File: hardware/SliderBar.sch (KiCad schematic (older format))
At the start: 5 parts

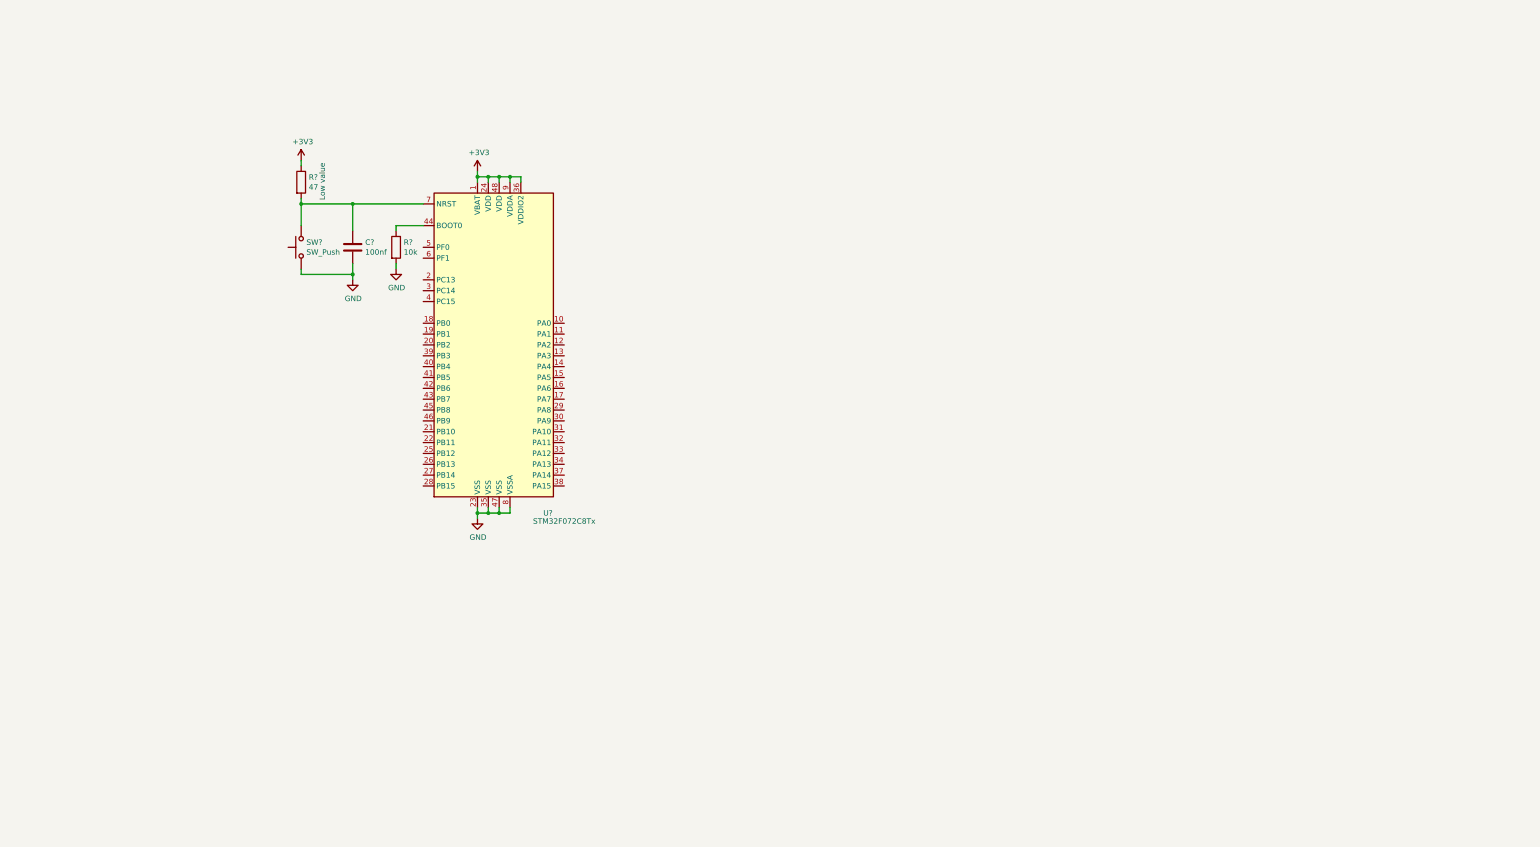
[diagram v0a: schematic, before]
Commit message: Add ULDO 3.3V regulator
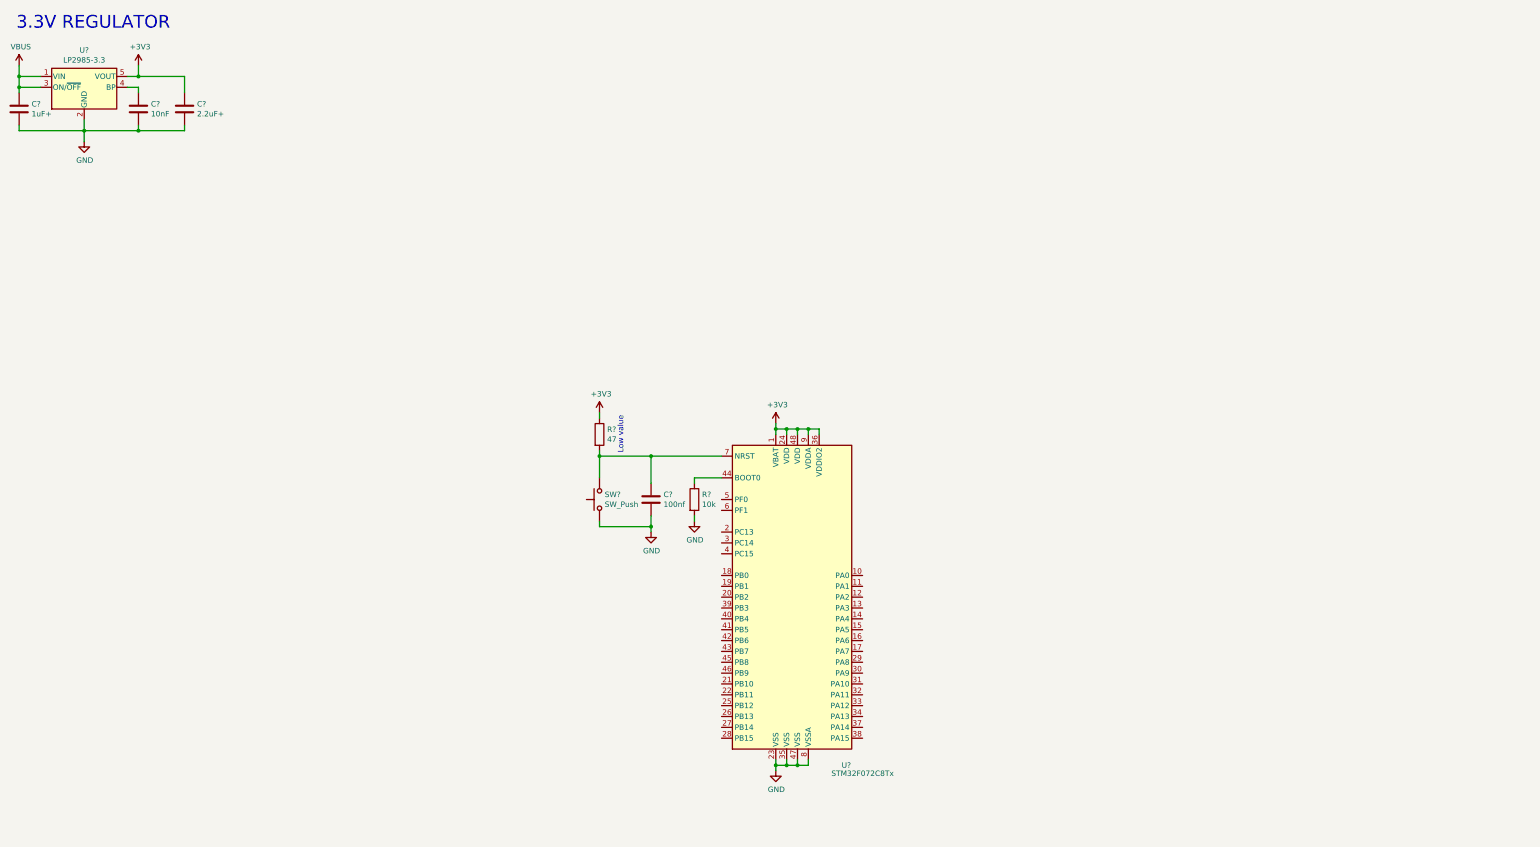
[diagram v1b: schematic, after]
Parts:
- added C?: 1uF+, symbol Device:C
- added C?: 10nF, symbol Device:C
- added C?: 2.2uF+, symbol Device:C
- added U?: LP2985-3.3, Package_TO_SOT_SMD:SOT-23-5, symbol Regulator_Linear:LP2985-3.3
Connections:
- net +3V3: now also C?.1, U?.5 (VOUT)
- net GND: now also C?.2, C?.2, C?.2, U?.2 (GND)
- new net: C?.1, U?.4 (BP)
- new net VBUS: C?.1, U?.1 (VIN), U?.3 (ON/~OFF~)
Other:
- note added: "3.3V REGULATOR"
- moved on the sheet: C?, R?, SW?, U?

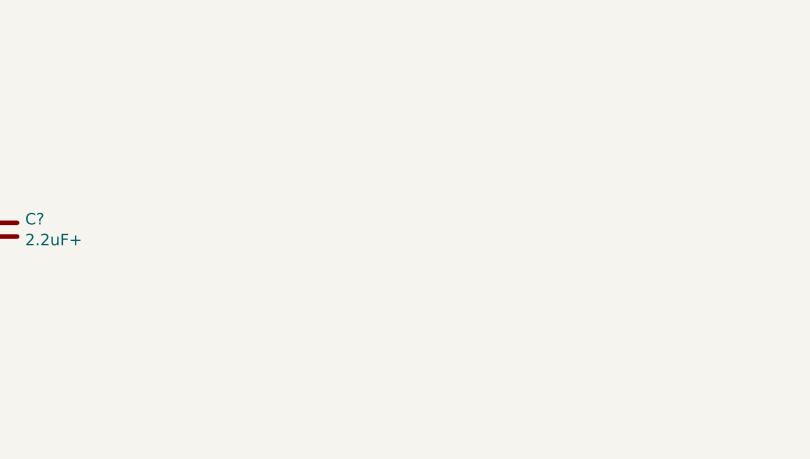
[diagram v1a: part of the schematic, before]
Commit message: Add power protection diodes
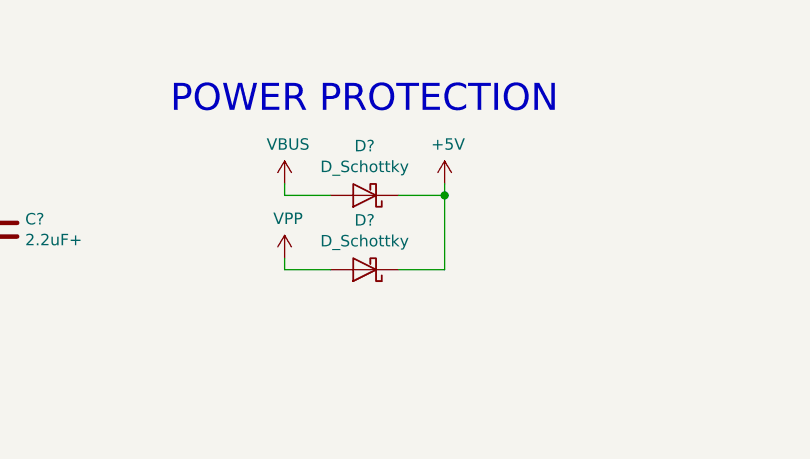
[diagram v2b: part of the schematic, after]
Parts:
- added D? (x2): D_Schottky, symbol Device:D_Schottky
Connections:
- net VBUS: now also D?.2 (A)
- new net +5V: D?.1 (K), D?.1 (K)
- new net VPP: D?.2 (A)
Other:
- note added: "POWER PROTECTION"
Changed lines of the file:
@@
 Text Notes 1300 950  0    118  ~ 0
 3.3V REGULATOR
+$Comp
+L power:VBUS #PWR?
+U 1 1 5D009DCE
+P 4100 1475
+F 0 "#PWR?" H 4100 1325 50  0001 C CNN
+F 1 "VBUS" H 4115 1648 50  0000 C CNN
+F 2 "" H 4100 1475 50  0001 C CNN
+F 3 "" H 4100 1475 50  0001 C CNN
+	1    4100 1475
+	1    0    0    -1
+$EndComp
+$Comp
+L power:VPP #PWR?
+U 1 1 5D00A59F
+P 4100 1800
+F 0 "#PWR?" H 4100 1650 50  0001 C CNN
+F 1 "VPP" H 4115 1973 50  0000 C CNN
+F 2 "" H 4100 1800 50  0001 C CNN
+F 3 "" H 4100 1800 50  0001 C CNN
+	1    4100 1800
+	1    0    0    -1
+$EndComp
+$Comp
+L Device:D_Schottky D?
+U 1 1 5D00B4CC
+P 4450 1525
+F 0 "D?" H 4450 1309 50  0000 C CNN
+F 1 "D_Schottky" H 4450 1400 50  0000 C CNN
+F 2 "" H 4450 1525 50  0001 C CNN
+F 3 "~" H 4450 1525 50  0001 C CNN
+	1    4450 1525
+	-1   0    0    1
+$EndComp
+$Comp
+L Device:D_Schottky D?
+U 1 1 5D00C48C
+P 4450 1850
+F 0 "D?" H 4450 1634 50  0000 C CNN
+F 1 "D_Schottky" H 4450 1725 50  0000 C CNN
+F 2 "" H 4450 1850 50  0001 C CNN
+F 3 "~" H 4450 1850 50  0001 C CNN
+	1    4450 1850
+	-1   0    0    1
+$EndComp
+Wire Wire Line
+	4100 1800 4100 1850
+Wire Wire Line
+	4100 1850 4300 1850
+Wire Wire Line
+	4100 1475 4100 1525
+Wire Wire Line
+	4100 1525 4300 1525
+$Comp
+L power:+5V #PWR?
+U 1 1 5D01175F
+P 4800 1475
+F 0 "#PWR?" H 4800 1325 50  0001 C CNN
+F 1 "+5V" H 4815 1648 50  0000 C CNN
+F 2 "" H 4800 1475 50  0001 C CNN
+F 3 "" H 4800 1475 50  0001 C CNN
+	1    4800 1475
+	1    0    0    -1
+$EndComp
+Wire Wire Line
+	4800 1475 4800 1525
+Wire Wire Line
+	4800 1525 4600 1525
+Wire Wire Line
+	4600 1850 4800 1850
+Wire Wire Line
+	4800 1850 4800 1525
+Connection ~ 4800 1525
+Text Notes 3600 1175 0    118  ~ 0
+POWER PROTECTION
 $EndSCHEMATC

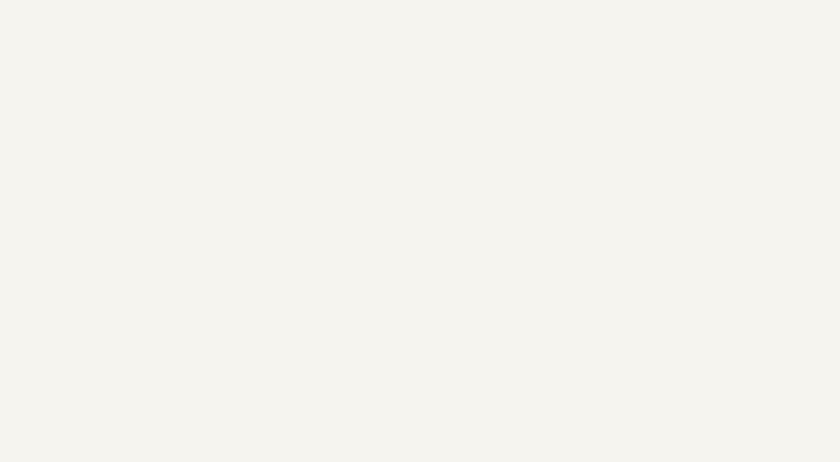
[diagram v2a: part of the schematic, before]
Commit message: Add decoupling caps
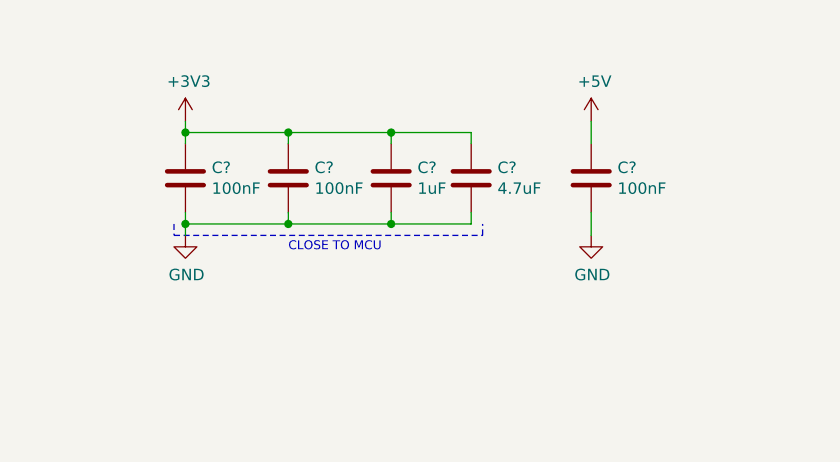
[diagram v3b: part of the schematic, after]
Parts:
- added C? (x3): 100nF, symbol Device:C
- added C?: 1uF, symbol Device:C
- added C?: 4.7uF, symbol Device:C
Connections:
- net +3V3: now also C?.1, C?.1, C?.1, C?.1
- net +5V: now also C?.1
- net GND: now also C?.2, C?.2, C?.2, C?.2, C?.2
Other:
- note added: "CLOSE TO MCU"
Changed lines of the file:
@@
 Text Notes 3600 1175 0    118  ~ 0
 POWER PROTECTION
+$Comp
+L power:+3V3 #PWR?
+U 1 1 5CFE80E6
+P 6175 1200
+F 0 "#PWR?" H 6175 1050 50  0001 C CNN
+F 1 "+3V3" H 6190 1373 50  0000 C CNN
+F 2 "" H 6175 1200 50  0001 C CNN
+F 3 "" H 6175 1200 50  0001 C CNN
+	1    6175 1200
+	1    0    0    -1
+$EndComp
+$Comp
+L power:GND #PWR?
+U 1 1 5CFE87EA
+P 6175 1700
+F 0 "#PWR?" H 6175 1450 50  0001 C CNN
+F 1 "GND" H 6180 1527 50  0000 C CNN
+F 2 "" H 6175 1700 50  0001 C CNN
+F 3 "" H 6175 1700 50  0001 C CNN
+	1    6175 1700
+	1    0    0    -1
+$EndComp
+$Comp
+L power:+5V #PWR?
+U 1 1 5CFE8FF3
+P 7950 1200
+F 0 "#PWR?" H 7950 1050 50  0001 C CNN
+F 1 "+5V" H 7965 1373 50  0000 C CNN
+F 2 "" H 7950 1200 50  0001 C CNN
+F 3 "" H 7950 1200 50  0001 C CNN
+	1    7950 1200
+	1    0    0    -1
+$EndComp
+$Comp
+L power:GND #PWR?
+U 1 1 5CFE94C3
+P 7950 1700
+F 0 "#PWR?" H 7950 1450 50  0001 C CNN
+F 1 "GND" H 7955 1527 50  0000 C CNN
+F 2 "" H 7950 1700 50  0001 C CNN
+F 3 "" H 7950 1700 50  0001 C CNN
+	1    7950 1700
+	1    0    0    -1
+$EndComp
+$Comp
+L Device:C C?
+U 1 1 5CFE9B17
+P 6175 1450
+F 0 "C?" H 6290 1496 50  0000 L CNN
+F 1 "100nF" H 6290 1405 50  0000 L CNN
+F 2 "" H 6213 1300 50  0001 C CNN
+F 3 "~" H 6175 1450 50  0001 C CNN
+	1    6175 1450
+	1    0    0    -1
+$EndComp
+$Comp
+L Device:C C?
+U 1 1 5CFEA76C
+P 6625 1450
+F 0 "C?" H 6740 1496 50  0000 L CNN
+F 1 "100nF" H 6740 1405 50  0000 L CNN
+F 2 "" H 6663 1300 50  0001 C CNN
+F 3 "~" H 6625 1450 50  0001 C CNN
+	1    6625 1450
+	1    0    0    -1
+$EndComp
+$Comp
+L Device:C C?
+U 1 1 5CFEAB56
+P 7075 1450
+F 0 "C?" H 7190 1496 50  0000 L CNN
+F 1 "1uF" H 7190 1405 50  0000 L CNN
+F 2 "" H 7113 1300 50  0001 C CNN
+F 3 "~" H 7075 1450 50  0001 C CNN
+	1    7075 1450
+	1    0    0    -1
+$EndComp
+$Comp
+L Device:C C?
+U 1 1 5CFEAFB3
+P 7425 1450
+F 0 "C?" H 7540 1496 50  0000 L CNN
+F 1 "4.7uF" H 7540 1405 50  0000 L CNN
+F 2 "" H 7463 1300 50  0001 C CNN
+F 3 "~" H 7425 1450 50  0001 C CNN
+	1    7425 1450
+	1    0    0    -1
+$EndComp
+$Comp
+L Device:C C?
+U 1 1 5CFEB2FD
+P 7950 1450
+F 0 "C?" H 8065 1496 50  0000 L CNN
+F 1 "100nF" H 8065 1405 50  0000 L CNN
+F 2 "" H 7988 1300 50  0001 C CNN
+F 3 "~" H 7950 1450 50  0001 C CNN
+	1    7950 1450
+	1    0    0    -1
+$EndComp
+Wire Wire Line
+	6175 1200 6175 1250
+Wire Wire Line
+	6625 1300 6625 1250
+Wire Wire Line
+	6625 1250 6175 1250
+Connection ~ 6175 1250
+Wire Wire Line
+	6175 1250 6175 1300
+Wire Wire Line
+	7075 1300 7075 1250
+Wire Wire Line
+	7075 1250 6625 1250
+Connection ~ 6625 1250
+Wire Wire Line
+	7425 1250 7075 1250
+Connection ~ 7075 1250
+Wire Wire Line
+	6175 1600 6175 1650
+Wire Wire Line
+	6625 1600 6625 1650
+Wire Wire Line
+	6625 1650 6175 1650
+Connection ~ 6175 1650
+Wire Wire Line
+	6175 1650 6175 1700
+Wire Wire Line
+	7075 1600 7075 1650
+Wire Wire Line
+	7075 1650 6625 1650
+Connection ~ 6625 1650
+Wire Wire Line
+	7425 1600 7425 1650
+Wire Wire Line
+	7425 1650 7075 1650
+Connection ~ 7075 1650
+Wire Wire Line
+	7425 1250 7425 1300
+Wire Wire Line
+	7950 1300 7950 1200
+Wire Wire Line
+	7950 1700 7950 1600
+Wire Notes Line width 12 style solid
+	6125 1650 6125 1700
+Wire Notes Line width 12 style solid
+	6125 1700 7475 1700
+Wire Notes Line width 12 style solid
+	7475 1700 7475 1650
+Text Notes 6625 1775 0    39   ~ 0
+CLOSE TO MCU
 $EndSCHEMATC

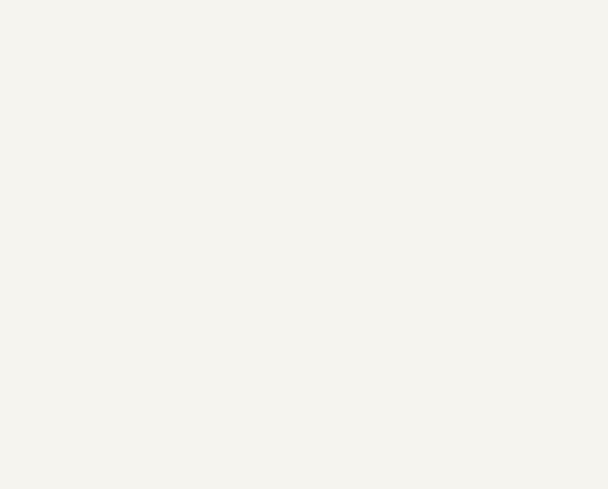
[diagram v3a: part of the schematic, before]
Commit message: Add USB connector
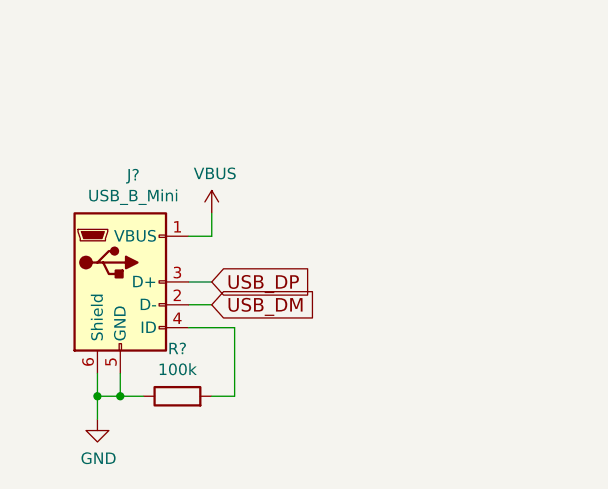
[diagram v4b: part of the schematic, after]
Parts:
- added J?: USB_B_Mini, symbol Connector:USB_B_Mini
- added R?: 100k, symbol Device:R
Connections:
- net GND: now also J?.5 (GND), J?.6 (Shield), R?.1
- net VBUS: now also J?.1 (VBUS)
- new net: J?.4 (ID), R?.2
- new net USB_DM: J?.2 (D-)
- new net USB_DP: J?.3 (D+)
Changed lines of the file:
@@
 Text Notes 6625 1775 0    39   ~ 0
 CLOSE TO MCU
+Text GLabel 2075 7575 2    59   Input ~ 0
+USB_DP
+Text GLabel 2075 7675 2    59   Input ~ 0
+USB_DM
+$Comp
+L power:VBUS #PWR?
+U 1 1 5D00D8E3
+P 2075 7275
+F 0 "#PWR?" H 2075 7125 50  0001 C CNN
+F 1 "VBUS" H 2090 7448 50  0000 C CNN
+F 2 "" H 2075 7275 50  0001 C CNN
+F 3 "" H 2075 7275 50  0001 C CNN
+	1    2075 7275
+	1    0    0    -1
+$EndComp
+$Comp
+L Connector:USB_B_Mini J?
+U 1 1 5D010FF8
+P 1675 7575
+F 0 "J?" H 1732 8042 50  0000 C CNN
+F 1 "USB_B_Mini" H 1732 7951 50  0000 C CNN
+F 2 "" H 1825 7525 50  0001 C CNN
+F 3 "~" H 1825 7525 50  0001 C CNN
+	1    1675 7575
+	1    0    0    -1
+$EndComp
+$Comp
+L Device:R R?
+U 1 1 5D01368F
+P 1925 8075
+F 0 "R?" V 2132 8075 50  0000 C CNN
+F 1 "100k" V 2041 8075 50  0000 C CNN
+F 2 "" V 1855 8075 50  0001 C CNN
+F 3 "~" H 1925 8075 50  0001 C CNN
+	1    1925 8075
+	0    -1   -1   0
+$EndComp
+Wire Wire Line
+	1975 7675 2075 7675
+Wire Wire Line
+	2075 7575 1975 7575
+Wire Wire Line
+	1975 7375 2075 7375
+Wire Wire Line
+	2075 7375 2075 7275
+$Comp
+L power:GND #PWR?
+U 1 1 5D01A8DC
+P 1575 8175
+F 0 "#PWR?" H 1575 7925 50  0001 C CNN
+F 1 "GND" H 1580 8002 50  0000 C CNN
+F 2 "" H 1575 8175 50  0001 C CNN
+F 3 "" H 1575 8175 50  0001 C CNN
+	1    1575 8175
+	1    0    0    -1
+$EndComp
+Wire Wire Line
+	1975 7775 2175 7775
+Wire Wire Line
+	2175 7775 2175 8075
+Wire Wire Line
+	2175 8075 2075 8075
+Wire Wire Line
+	1775 8075 1675 8075
+Wire Wire Line
+	1575 8075 1575 8175
+Wire Wire Line
+	1575 7975 1575 8075
+Connection ~ 1575 8075
+Wire Wire Line
+	1675 7975 1675 8075
+Connection ~ 1675 8075
+Wire Wire Line
+	1675 8075 1575 8075
 $EndSCHEMATC

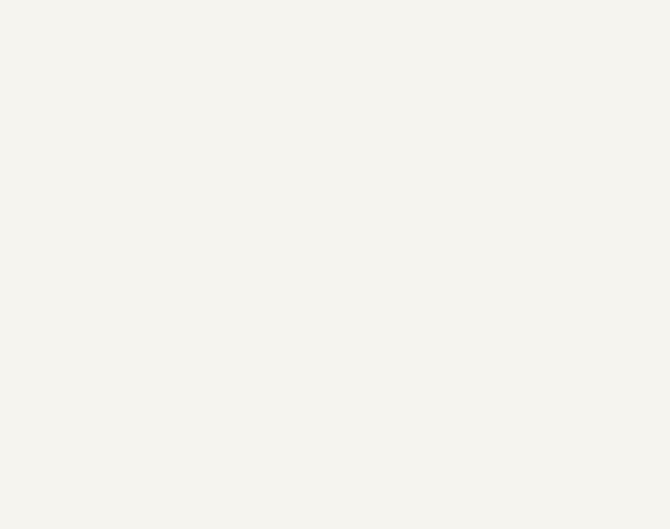
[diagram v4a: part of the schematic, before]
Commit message: Add motor driver with current limiting
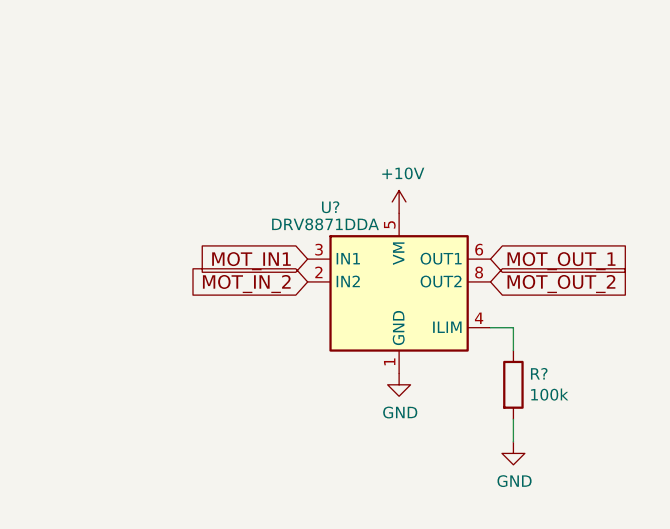
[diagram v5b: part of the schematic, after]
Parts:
- added R?: 100k, symbol Device:R
- added U?: DRV8871DDA, Package_SO:Texas_HTSOP-8-1EP_3.9x4.9mm_P1.27mm_EP2.95x4.9mm_Mask2.4x3.1mm_ThermalVias, symbol Driver_Motor:DRV8871DDA
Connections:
- net GND: now also R?.2, U?.1 (GND), U?.7 (GND), U?.9 (GND)
- new net: R?.1, U?.4 (ILIM)
- new net +10V: U?.5 (VM)
- new net MOT_IN1: U?.3 (IN1)
- new net MOT_IN_2: U?.2 (IN2)
- new net MOT_OUT_1: U?.6 (OUT1)
- new net MOT_OUT_2: U?.8 (OUT2)
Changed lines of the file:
@@
 Wire Wire Line
 	1675 8075 1575 8075
+$Comp
+L Driver_Motor:DRV8871DDA U?
+U 1 1 5D02679F
+P 13375 7400
+F 0 "U?" H 13075 7725 50  0000 C CNN
+F 1 "DRV8871DDA" H 13050 7650 50  0000 C CNN
+F 2 "Package_SO:Texas_HTSOP-8-1EP_3.9x4.9mm_P1.27mm_EP2.95x4.9mm_Mask2.4x3.1mm_ThermalVias" H 13625 7350 50  0001 C CNN
+F 3 "http://www.ti.com/lit/ds/symlink/drv8871.pdf" H 13625 7350 50  0001 C CNN
+	1    13375 7400
+	1    0    0    -1
+$EndComp
+Text GLabel 13775 7300 2    59   Input ~ 0
+MOT_OUT_1
+Text GLabel 13775 7400 2    59   Input ~ 0
+MOT_OUT_2
+Text GLabel 12975 7300 0    59   Input ~ 0
+MOT_IN1
+Text GLabel 12975 7400 0    59   Input ~ 0
+MOT_IN_2
+$Comp
+L power:+10V #PWR?
+U 1 1 5D0291A4
+P 13375 7100
+F 0 "#PWR?" H 13375 6950 50  0001 C CNN
+F 1 "+10V" H 13390 7273 50  0000 C CNN
+F 2 "" H 13375 7100 50  0001 C CNN
+F 3 "" H 13375 7100 50  0001 C CNN
+	1    13375 7100
+	1    0    0    -1
+$EndComp
+$Comp
+L power:GND #PWR?
+U 1 1 5D029EEB
+P 13375 7800
+F 0 "#PWR?" H 13375 7550 50  0001 C CNN
+F 1 "GND" H 13380 7627 50  0000 C CNN
+F 2 "" H 13375 7800 50  0001 C CNN
+F 3 "" H 13375 7800 50  0001 C CNN
+	1    13375 7800
+	1    0    0    -1
+$EndComp
+$Comp
+L Device:R R?
+U 1 1 5D02ABB0
+P 13875 7850
+F 0 "R?" H 13945 7896 50  0000 L CNN
+F 1 "100k" H 13945 7805 50  0000 L CNN
+F 2 "" V 13805 7850 50  0001 C CNN
+F 3 "~" H 13875 7850 50  0001 C CNN
+	1    13875 7850
+	1    0    0    -1
+$EndComp
+$Comp
+L power:GND #PWR?
+U 1 1 5D02B7F4
+P 13875 8100
+F 0 "#PWR?" H 13875 7850 50  0001 C CNN
+F 1 "GND" H 13880 7927 50  0000 C CNN
+F 2 "" H 13875 8100 50  0001 C CNN
+F 3 "" H 13875 8100 50  0001 C CNN
+	1    13875 8100
+	1    0    0    -1
+$EndComp
+Wire Wire Line
+	13875 8000 13875 8100
+Wire Wire Line
+	13875 7700 13875 7600
+Wire Wire Line
+	13875 7600 13775 7600
 $EndSCHEMATC

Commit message: Remove units from passive components values
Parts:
- C?: value 100nf -> 100n
- C?: value 1uF+ -> 1u+
- C?: value 10nF -> 10n
- C?: value 2.2uF+ -> 2.2u+
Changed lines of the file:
@@
 P 7150 5275
 F 0 "C?" H 7265 5321 50  0000 L CNN
-F 1 "100nf" H 7265 5230 50  0000 L CNN
+F 1 "100n" H 7265 5230 50  0000 L CNN
 F 2 "" H 7188 5125 50  0001 C CNN
 F 3 "~" H 7150 5275 50  0001 C CNN
@@
 P 1325 1675
 F 0 "C?" H 1440 1721 50  0000 L CNN
-F 1 "1uF+" H 1440 1630 50  0000 L CNN
+F 1 "1u+" H 1440 1630 50  0000 L CNN
 F 2 "" H 1363 1525 50  0001 C CNN
 F 3 "~" H 1325 1675 50  0001 C CNN
@@
 P 2425 1675
 F 0 "C?" H 2540 1721 50  0000 L CNN
-F 1 "10nF" H 2540 1630 50  0000 L CNN
+F 1 "10n" H 2540 1630 50  0000 L CNN
 F 2 "" H 2463 1525 50  0001 C CNN
 F 3 "~" H 2425 1675 50  0001 C CNN
@@
 P 2850 1675
 F 0 "C?" H 2965 1721 50  0000 L CNN
-F 1 "2.2uF+" H 2965 1630 50  0000 L CNN
+F 1 "2.2u+" H 2965 1630 50  0000 L CNN
 F 2 "" H 2888 1525 50  0001 C CNN
 F 3 "~" H 2850 1675 50  0001 C CNN
